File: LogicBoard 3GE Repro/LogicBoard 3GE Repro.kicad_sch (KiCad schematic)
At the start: 165 parts, among them IC201 2363, IC202 74LS00, IC203 74LS32, IC204 2114, IC205 2114, IC206 68A09, IC207 6522, IC208 AY3-8912, IC301 MC1408, IC302 CD4052B, IC303 LF347, IC304 LF353, IC305 4066, J201 CART, J202 DB9_Male, J203 DB9_Male, J204 Power, J301 Video, J302 Audio, Q301 2N3905, Q302 2N3905, Q303 2N3904, SW201 Reset, Y201 6MHz

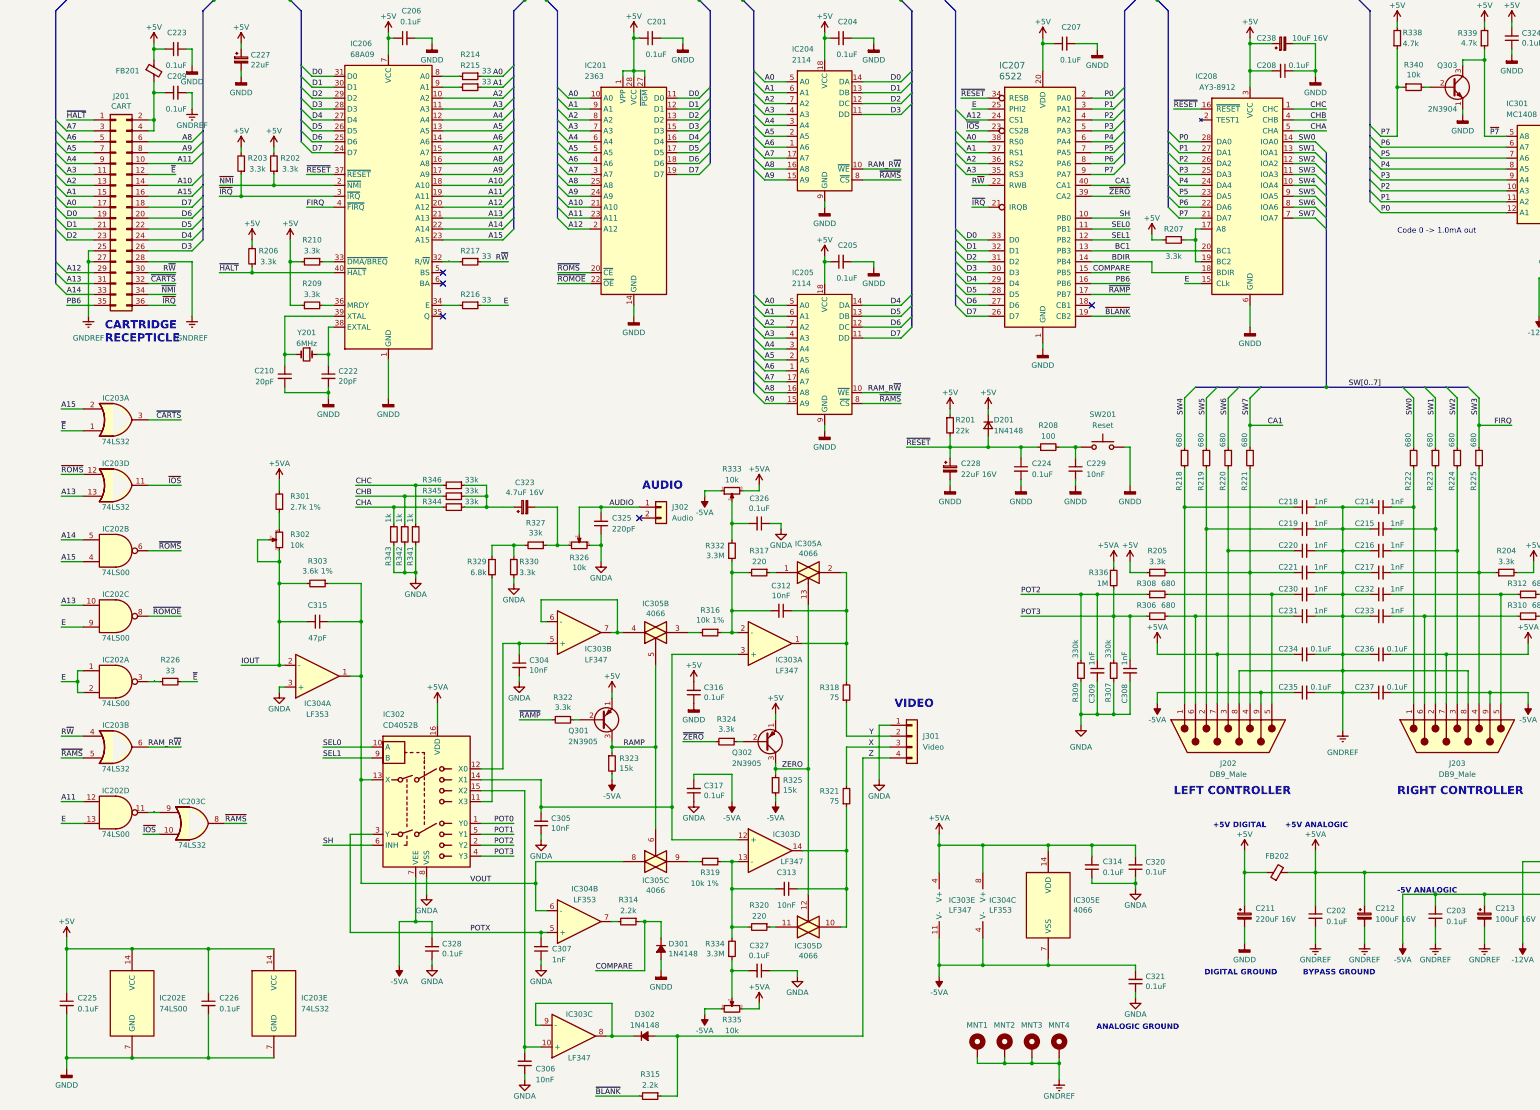
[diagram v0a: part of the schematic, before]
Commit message: Repro capture: GAL placed + wired, library file restored, ERC 290->81
- ATF16V8 (U1) placed and wired: decode + nE(=!E) for cart J201.12, C239 decap
- Added missing 'Vectrex LogicBoard.kicad_sym' (extracted from schematic cache)
  -> clears 32 lib_symbol_issues without introducing mismatches
- Update Symbols from Library done correctly (fields/refs preserved)
- .pld: added nE output for the cartridge inverted-E clock

Co-Authored-By: Claude Opus 4.8 <noreply@anthropic.com>
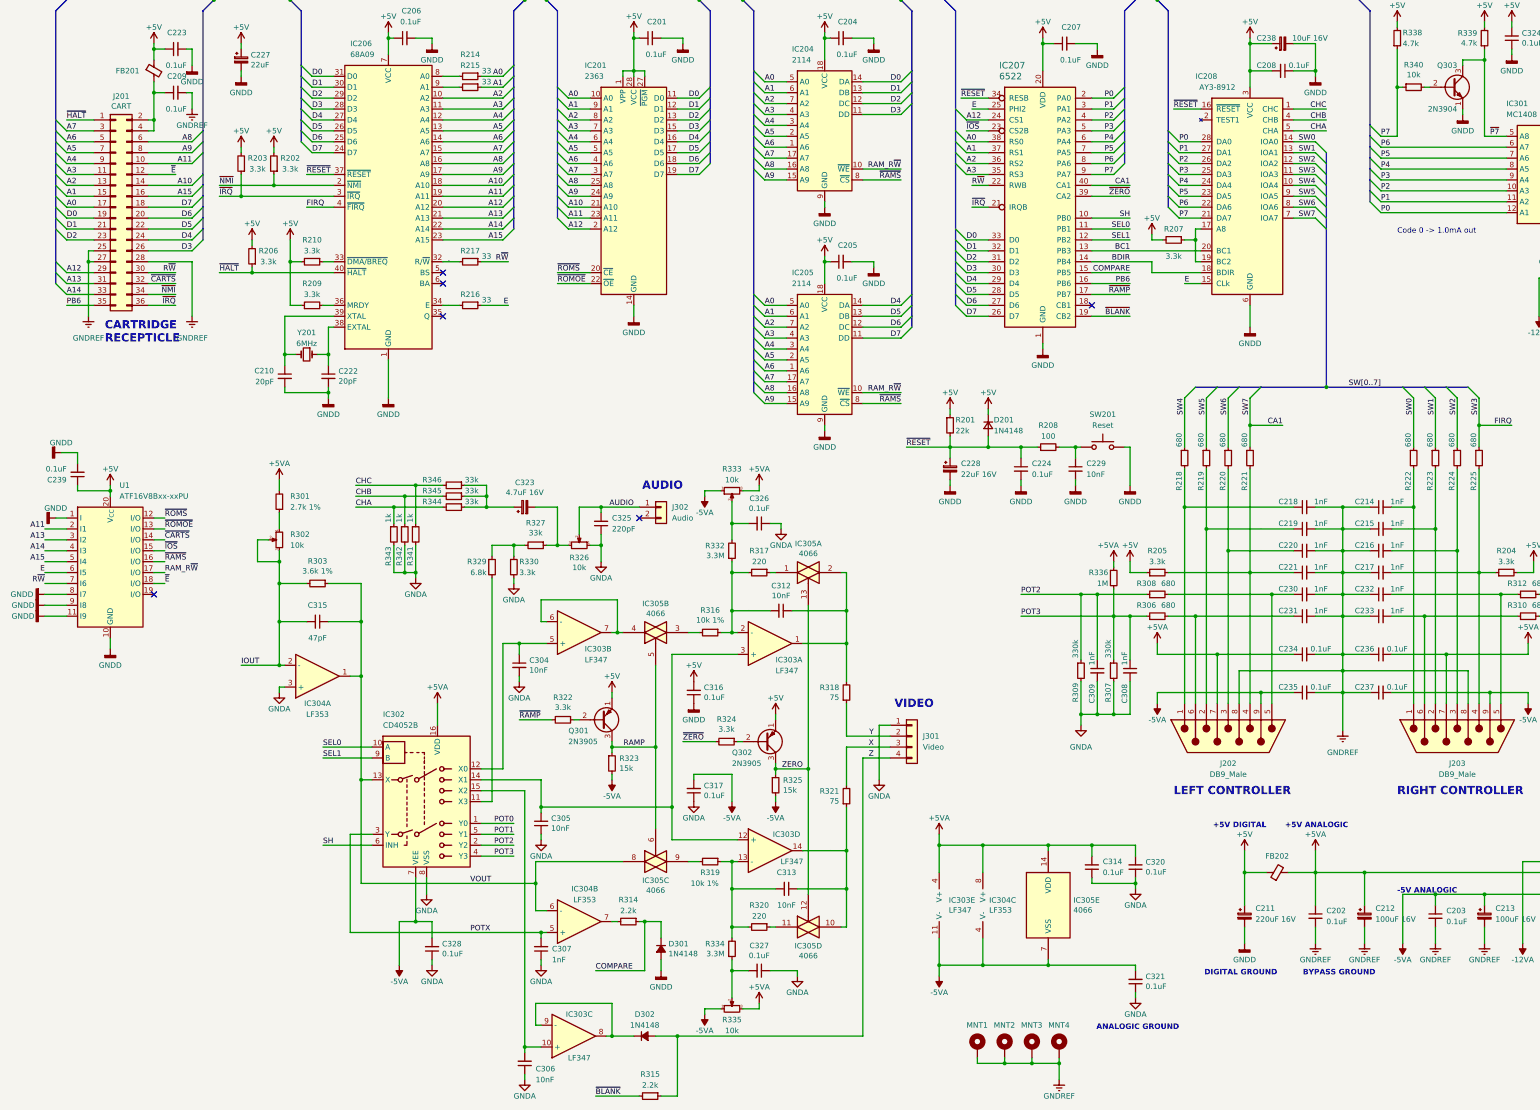
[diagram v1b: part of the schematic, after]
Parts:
- removed C225, C226: 0.1uF, Capacitor_THT:C_Disc_D5.0mm_W2.5mm_P5.00mm, symbol Device:C_Small
- removed IC202: 74LS00, Package_DIP:DIP-14_W7.62mm, symbol 74xx:74LS00
- removed IC203: 74LS32, Package_DIP:DIP-14_W7.62mm, symbol 74xx:74LS32
- removed R226: 33, Vectrex LogicBoard:R_Axial_DIN0207_L6.3mm_D2.5mm_P12.70mm_Horizontal, symbol Device:R_Small
- added C239: 0.1uF, Capacitor_THT:C_Disc_D5.0mm_W2.5mm_P5.00mm, symbol Device:C_Small
- added U1: ATF16V8Bxx-xxPU, Package_DIP:DIP-20_W7.62mm, symbol Logic_Programmable:ATF16V8Bxx-xxPU
- Q301, Q302, Q303: footprint Package_TO_SOT_THT:TO-92_Wide -> Package_TO_SOT_THT:TO-92_Inline
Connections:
- net +5V: now also C239.1, U1.20 (V_{CC})
- net A11: now also U1.2 (I1)
- net A13: now also U1.3 (I2)
- net A14: now also U1.4 (I3)
- net A15: now also U1.5 (I4)
- net E: now also U1.6 (I5)
- net GNDD: now also C239.2, U1.1 (I), U1.10 (GND), U1.11 (I9), U1.8 (I7), U1.9 (I8)
- net RAM_R~{W}: now also U1.17 (I/O)
- net R~{W}: now also U1.7 (I6)
- net ~{CARTS}: now also U1.14 (I/O)
- net ~{E}: now also U1.18 (I/O)
- net ~{IOS}: now also U1.15 (I/O)
- net ~{RAMS}: now also U1.16 (I/O)
- net ~{ROMOE}: now also U1.13 (I/O)
- net ~{ROMS}: now also U1.12 (I/O)
- no-connect marks 5 -> 6

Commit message: Repro: ROM substitution - 27C512PLCC (IC201) + JP1-3 bank jumpers
Replaced 27C64 with stock Memory_EPROM:27C512PLCC (old repro's symbol was
broken - missing A1/A9). A0-A12+D0-D7 to bus, CE=ROMS, OE=ROMOE; A13/14/15
to 3-pin jumpers (+5V/GND select, never floats). ERC 15->12.

Co-Authored-By: Claude Opus 4.8 <noreply@anthropic.com>
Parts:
- removed IC201: 2363, Package_DIP:DIP-28_W15.24mm, symbol Vectrex LogicBoard:27C64
- added IC201: 27C512PLCC, Package_LCC:PLCC-32_11.4x14.0mm_P1.27mm, symbol Memory_EPROM:27C512PLCC
- added JP1, JP2, JP3: Jumper_3_Bridged12, symbol Jumper:Jumper_3_Bridged12
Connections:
- net +5V: now also IC201.32 (VCC), JP1.1 (A), JP2.1 (A), JP3.1 (A)
- net A0: now also IC201.11 (A0)
- net A1: now also IC201.10 (A1)
- net A10: now also IC201.24 (A10)
- net A11: now also IC201.27 (A11)
- net A12: now also IC201.3 (A12)
- net A2: now also IC201.9 (A2)
- net A3: now also IC201.8 (A3)
- net A4: now also IC201.7 (A4)
- net A5: now also IC201.6 (A5)
- net A6: now also IC201.5 (A6)
- net A7: now also IC201.4 (A7)
- net A8: now also IC201.29 (A8)
- net A9: now also IC201.28 (A9)
- net D0: now also IC201.13 (O0)
- net D1: now also IC201.14 (O1)
- net D2: now also IC201.15 (O2)
- net D3: now also IC201.18 (O3)
- net D4: now also IC201.19 (O4)
- net D5: now also IC201.20 (O5)
- net D6: now also IC201.21 (O6)
- net D7: now also IC201.22 (O7)
- net GNDD: now also IC201.16 (GND), JP1.3 (B), JP2.3 (B), JP3.3 (B)
- net ~{ROMOE}: now also IC201.25 (~{OE}/VPP)
- net ~{ROMS}: now also IC201.23 (~{CE})
- new net ROM_BANK0: IC201.30 (A13), JP1.2 (C)
- new net ROM_BANK1: IC201.31 (A14), JP2.2 (C)
- new net ROM_BANK2: IC201.2 (A15), JP3.2 (C)

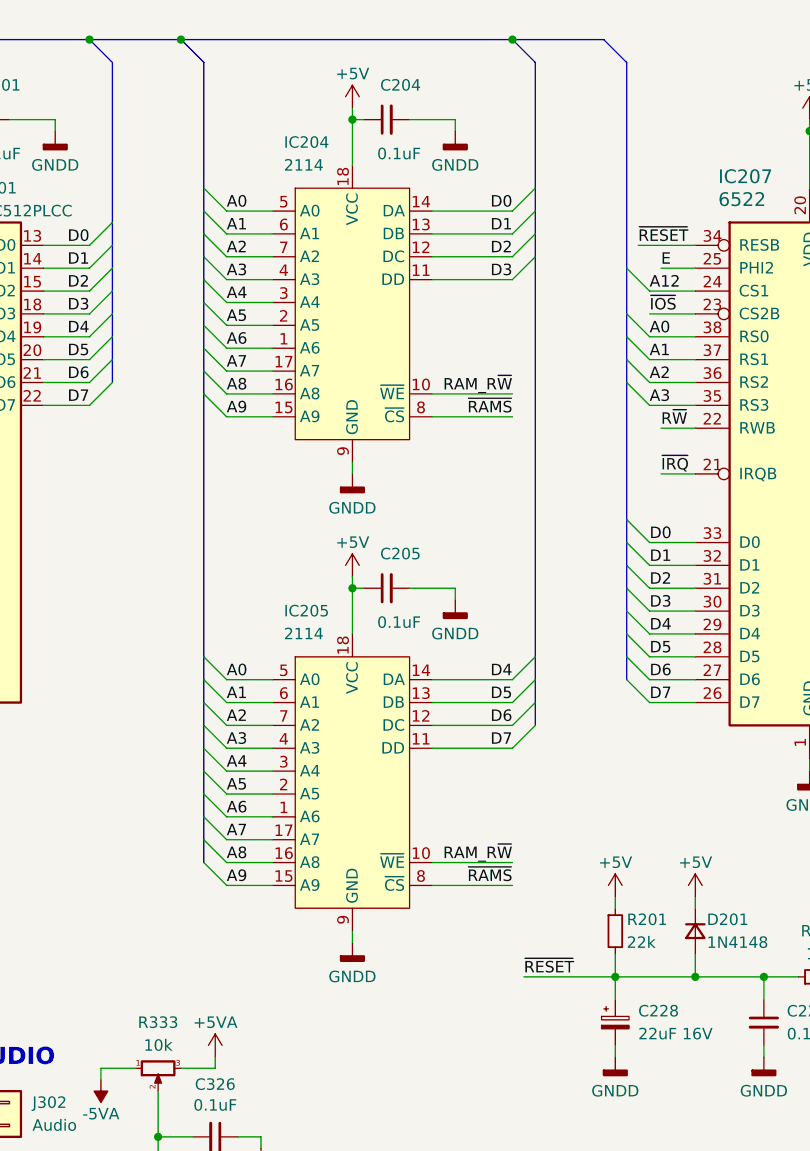
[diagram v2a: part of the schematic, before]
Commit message: Repro: RAM substitution - single CY62256 (IC204) replaces 2x 2114
Deleted IC204+IC205 (2114s), placed stock Memory_RAM:CY62256-70PC as IC204:
A0-A9 to bus, A10-A14 to GND, D0-D7, /CS=RAMS, /WE=RAM_R/W, /OE=GND. 0 errors.

Co-Authored-By: Claude Opus 4.8 <noreply@anthropic.com>
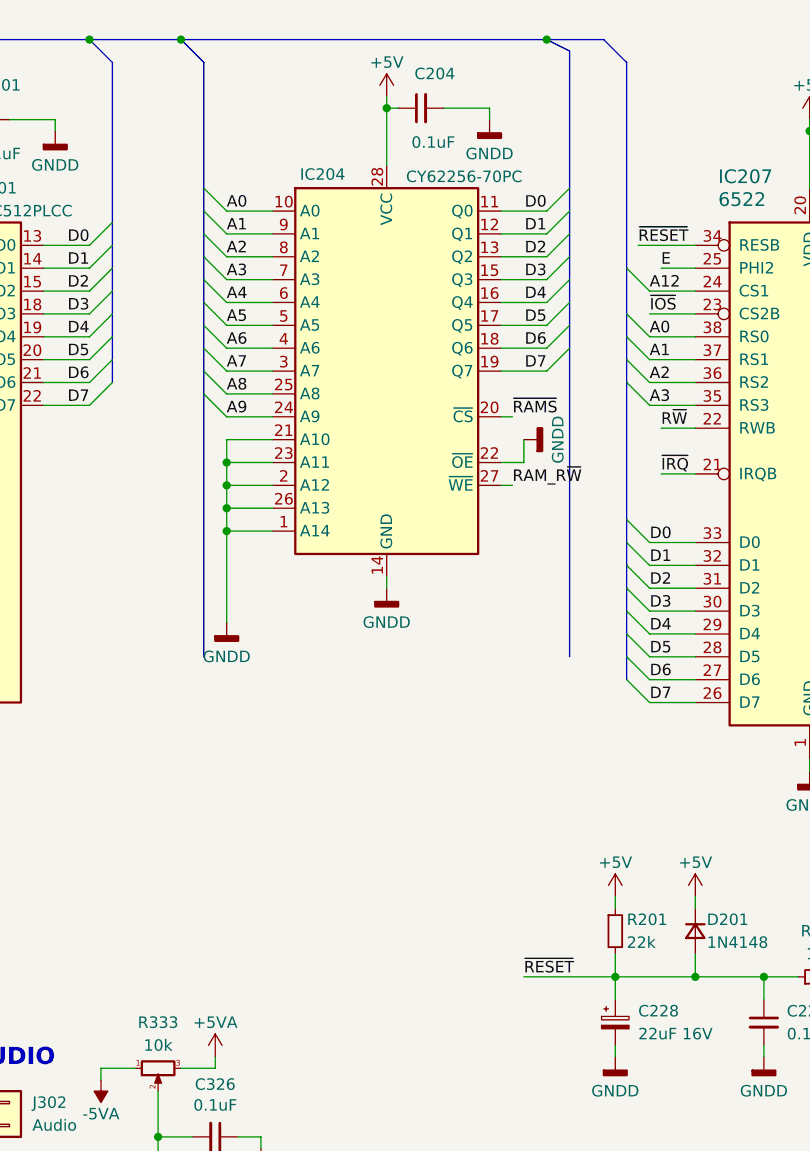
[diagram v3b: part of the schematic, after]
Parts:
- removed C205: 0.1uF, Capacitor_THT:C_Disc_D5.0mm_W2.5mm_P5.00mm, symbol Device:C_Small
- removed IC204, IC205: 2114, Package_DIP:DIP-18_W7.62mm, symbol Vectrex LogicBoard:2114
- added IC204: CY62256-70PC, Package_DIP:DIP-28_W15.24mm, symbol Memory_RAM:CY62256-70PC
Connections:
- net +5V: now also IC204.28 (VCC)
- net A0: now also IC204.10 (A0)
- net A1: now also IC204.9 (A1)
- net A2: now also IC204.8 (A2)
- net A3: now also IC204.7 (A3)
- net A4: now also IC204.6 (A4)
- net A5: now also IC204.5 (A5)
- net A6: now also IC204.4 (A6)
- net A7: now also IC204.3 (A7)
- net A8: now also IC204.25 (A8)
- net A9: now also IC204.24 (A9)
- net D0: now also IC204.11 (Q0)
- net D1: now also IC204.12 (Q1)
- net D2: now also IC204.13 (Q2)
- net D3: now also IC204.15 (Q3)
- net D4: now also IC204.16 (Q4)
- net D5: now also IC204.17 (Q5)
- net D6: now also IC204.18 (Q6)
- net D7: now also IC204.19 (Q7)
- net GNDD: now also IC204.1 (A14), IC204.14 (GND), IC204.2 (A12), IC204.21 (A10), IC204.22 (~{OE}), IC204.23 (A11), IC204.26 (A13)
- net RAM_R~{W}: now also IC204.27 (~{WE})
- net ~{RAMS}: now also IC204.20 (~{CS})
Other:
- moved on the sheet: C204

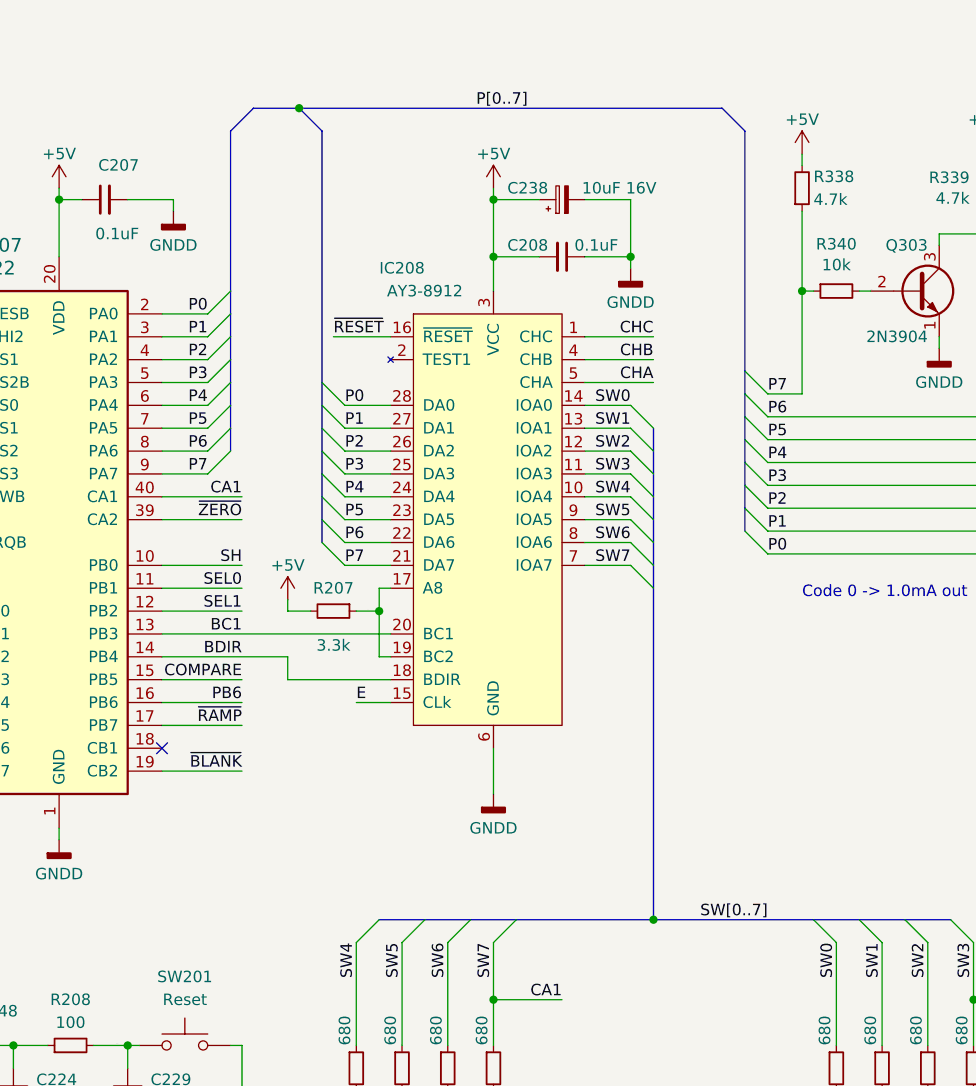
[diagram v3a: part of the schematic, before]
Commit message: Repro: sound substitution - YM2149 (IC208) replaces AY-3-8912
40-pin YM2149: port A=SW0-7, data=P0-7, BC1/BC2/BDIR/E/RESET, analog A/B/C.
TEST1=GND (clones), A8=+5V A9=GND SEL=+5V. R207 reconnected as BC2 pull-up.

Co-Authored-By: Claude Opus 4.8 <noreply@anthropic.com>
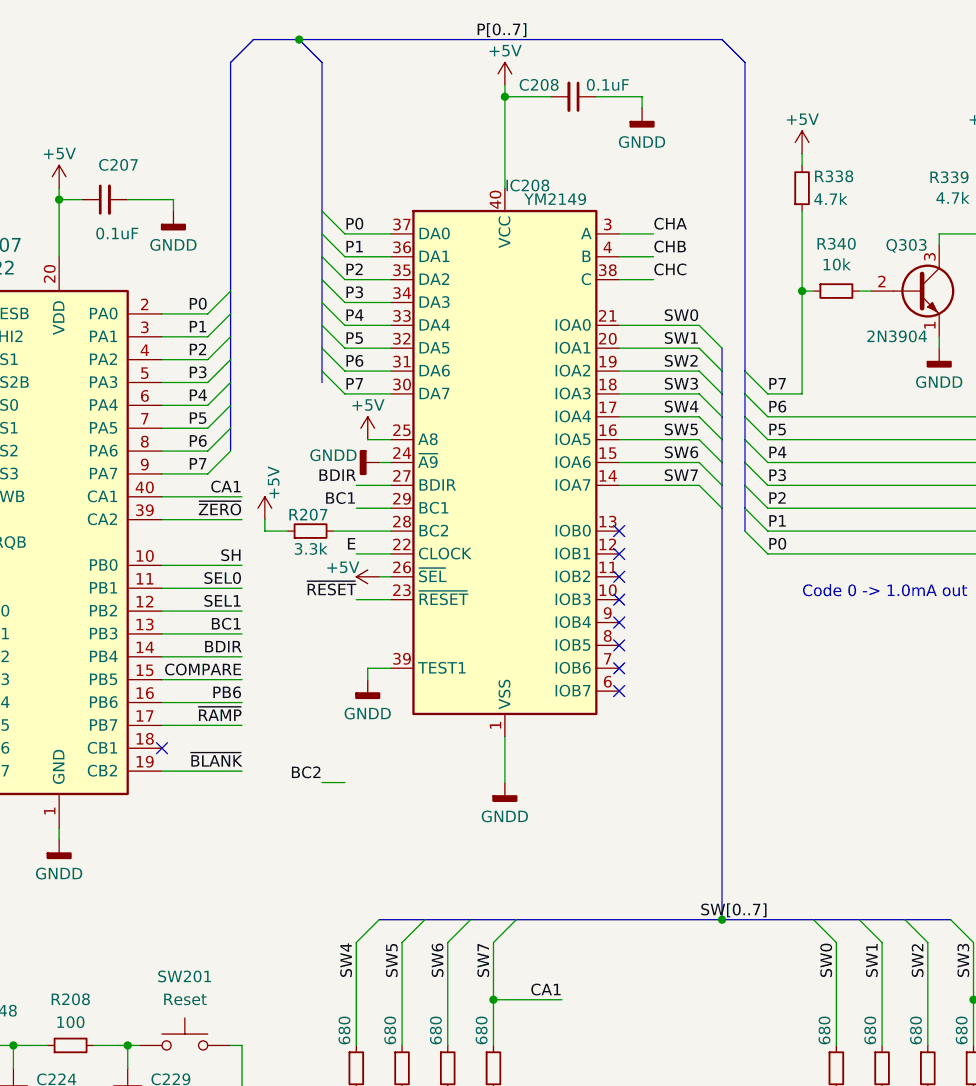
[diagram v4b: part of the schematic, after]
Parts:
- removed C238: 10uF 16V, Capacitor_THT:CP_Radial_Tantal_D5.0mm_P2.50mm, symbol Device:C_Polarized_Small
- removed IC208: AY3-8912, Package_DIP:DIP-28_W15.24mm, symbol Vectrex LogicBoard:AY3-8912
- added IC208: YM2149, Package_DIP:DIP-40_W15.24mm, symbol Audio:YM2149
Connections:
- net +5V: now also R207.1, IC208.25 (A8), IC208.26 (~{SEL}), IC208.40 (VCC); no longer R207.2
- net BC1: now also IC208.29 (BC1)
- net BC2: no longer R207.1
- net BDIR: now also IC208.27 (BDIR)
- net CA1: now also IC208.14 (IOA7)
- net CHA: now also IC208.3 (A)
- net CHB: now also IC208.4 (B)
- net CHC: now also IC208.38 (C)
- net E: now also IC208.22 (CLOCK)
- net FIRQ: now also IC208.18 (IOA3)
- net GNDD: now also IC208.1 (VSS), IC208.24 (~{A9}), IC208.39 (TEST1)
- net P0: now also IC208.37 (DA0)
- net P1: now also IC208.36 (DA1)
- net P2: now also IC208.35 (DA2)
- net P3: now also IC208.34 (DA3)
- net P4: now also IC208.33 (DA4)
- net P5: now also IC208.32 (DA5)
- net P6: now also IC208.31 (DA6)
- net P7: now also IC208.30 (DA7)
- net SW0: now also IC208.21 (IOA0)
- net SW1: now also IC208.20 (IOA1)
- net SW2: now also IC208.19 (IOA2)
- net SW4: now also IC208.17 (IOA4)
- net SW5: now also IC208.16 (IOA5)
- net SW6: now also IC208.15 (IOA6)
- net ~{RESET}: now also IC208.23 (~{RESET})
- new net: IC208.28 (BC2), R207.2
- no-connect marks 6 -> 14
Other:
- moved on the sheet: C208, R207
